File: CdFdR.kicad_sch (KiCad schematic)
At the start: 17 parts, among them J1 Moteur_1, J2 Moteur_2, J3 Moteur_3, J4 Moteur_4, U1 ESP32-S3-N16R8-DEVBOARD

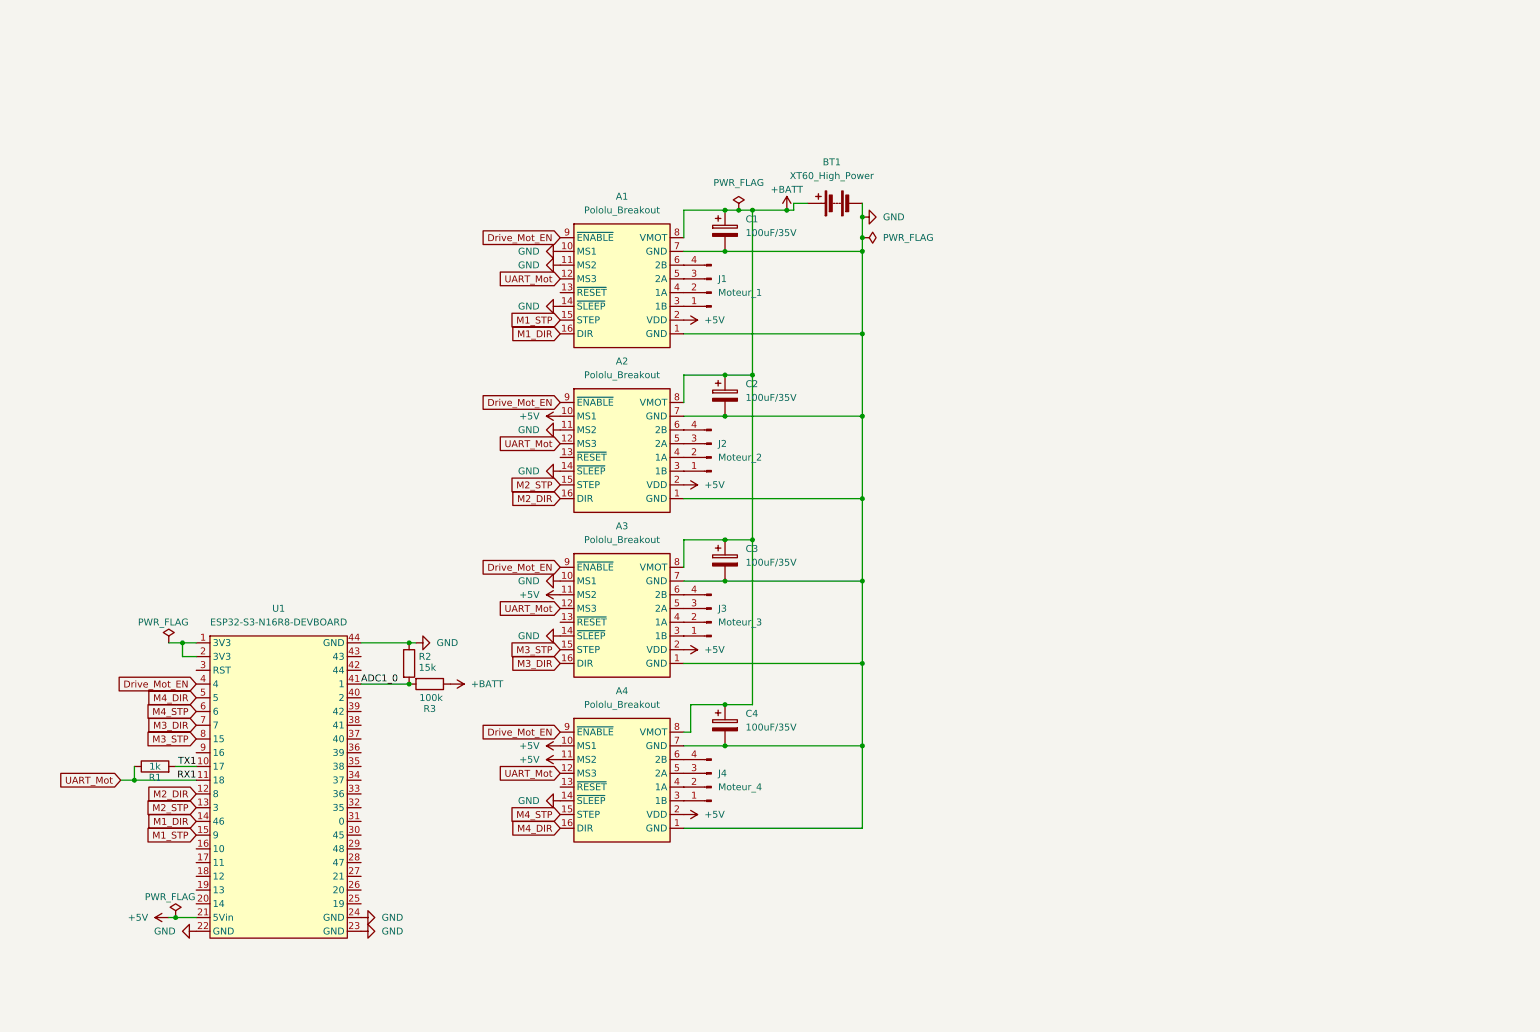
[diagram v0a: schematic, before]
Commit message: Ajout de composants
Ajout de composants sur le schématic
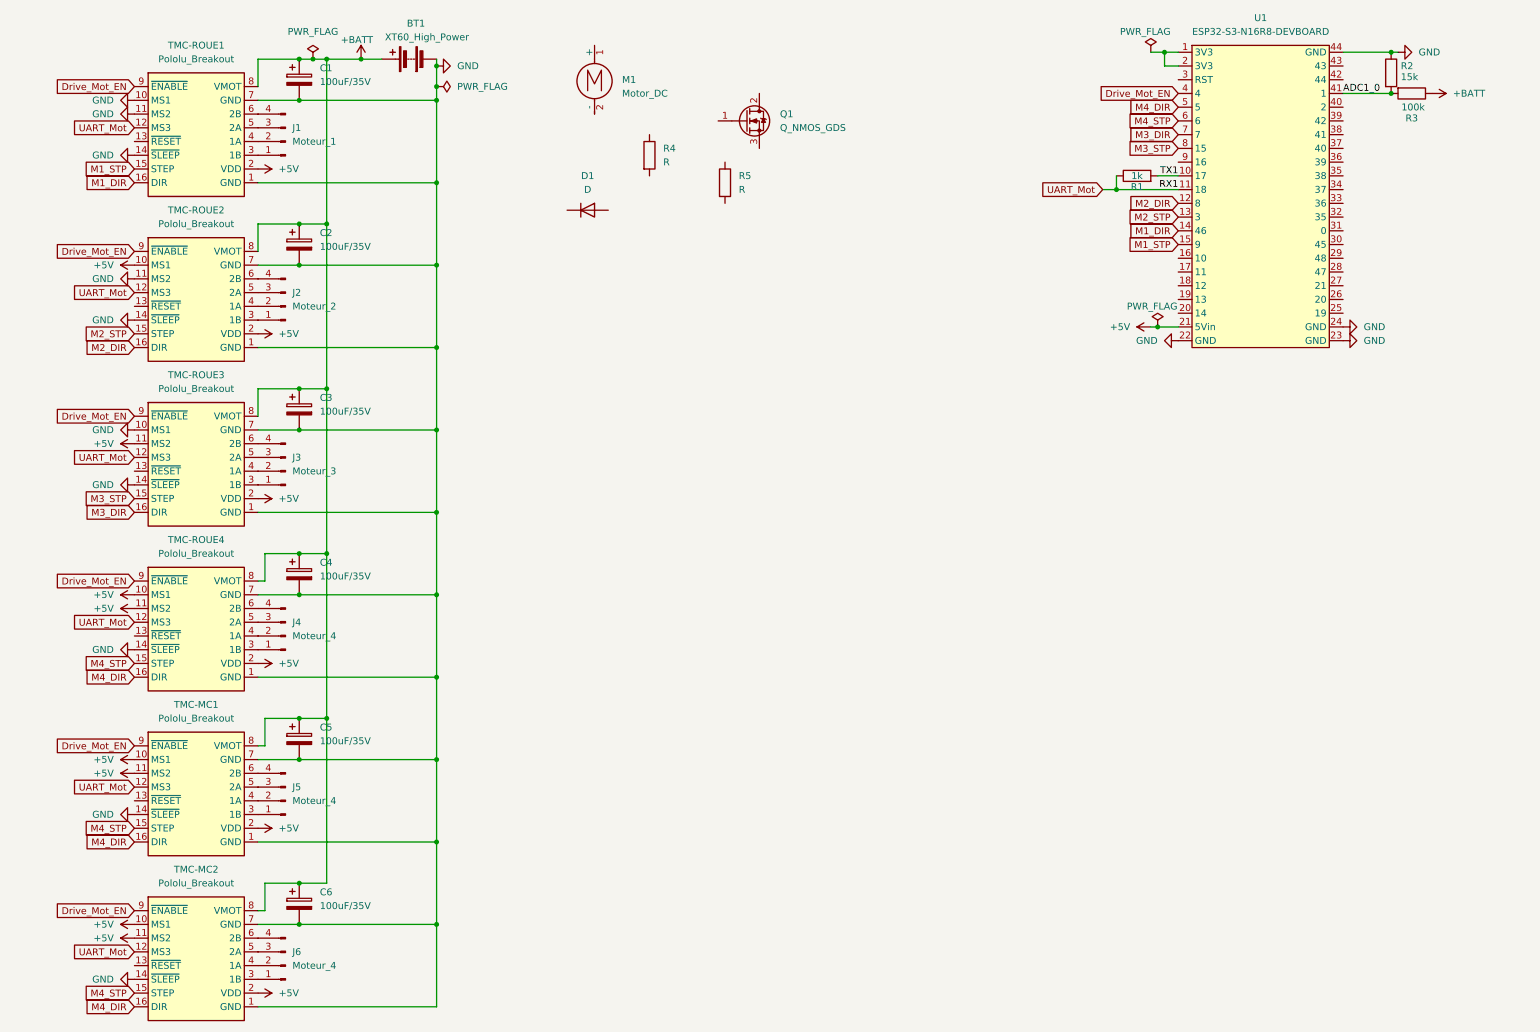
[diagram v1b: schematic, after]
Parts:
- added C5, C6: 100uF/35V, Capacitor_THT:CP_Radial_D6.3mm_P2.50mm, symbol Device:C_Polarized
- added D1: D, symbol Device:D
- added J5, J6: Moteur_4, Connector_PinHeader_2.54mm:PinHeader_1x04_P2.54mm_Vertical, symbol Connector:Conn_01x04_Pin
- added M1: Motor_DC, symbol Motor:Motor_DC
- added Q1: Q_NMOS_GDS, symbol Device:Q_NMOS_GDS
- added R4, R5: R, symbol Device:R
- added TMC-MC1, TMC-MC2: Pololu_Breakout, Custom:Pololu_Breakout-16_15.2x20.3mm_Better_Silkscreen, symbol Custom:Pololu_Breakout_Stepper_Driver
- renumbered A1 to TMC-ROUE1, A2 to TMC-ROUE2, A3 to TMC-ROUE3, A4 to TMC-ROUE4
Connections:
- net +5V: now also TMC-MC1.10 (MS1), TMC-MC1.11 (MS2), TMC-MC1.2 (VDD), TMC-MC2.10 (MS1), TMC-MC2.11 (MS2), TMC-MC2.2 (VDD)
- net +BATT: now also C5.1, C6.1, TMC-MC1.8 (VMOT), TMC-MC2.8 (VMOT)
- net Drive_Mot_EN: now also TMC-MC1.9 (~{ENABLE}), TMC-MC2.9 (~{ENABLE})
- net GND: now also C5.2, C6.2, TMC-MC1.1 (GND), TMC-MC1.14 (~{SLEEP}), TMC-MC1.7 (GND), TMC-MC2.1 (GND), TMC-MC2.14 (~{SLEEP}), TMC-MC2.7 (GND)
- net M4_DIR: now also TMC-MC1.16 (DIR), TMC-MC2.16 (DIR)
- net M4_STP: now also TMC-MC1.15 (STEP), TMC-MC2.15 (STEP)
- net UART_Mot: now also TMC-MC1.12 (MS3), TMC-MC2.12 (MS3)
- new net: J5.1 (Pin_1), TMC-MC1.3 (1B)
- new net: J5.2 (Pin_2), TMC-MC1.4 (1A)
- new net: J5.3 (Pin_3), TMC-MC1.5 (2A)
- new net: J5.4 (Pin_4), TMC-MC1.6 (2B)
- new net: J6.1 (Pin_1), TMC-MC2.3 (1B)
- new net: J6.2 (Pin_2), TMC-MC2.4 (1A)
- new net: J6.3 (Pin_3), TMC-MC2.5 (2A)
- new net: J6.4 (Pin_4), TMC-MC2.6 (2B)
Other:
- moved on the sheet: BT1, C1, C2, C3, C4, J1, J2, J3, J4, R1, R2, R3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

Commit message: Version envoyé pour vérif
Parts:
- removed M1: Motor_DC, symbol Motor:Motor_DC
- removed Q1: Q_NMOS_GDS, symbol Device:Q_NMOS_GDS
- added C7: 2200 uF, Capacitor_THT:CP_Radial_D16.0mm_P7.50mm, symbol Device:C_Polarized
- added D2, D3, D4: FR107, Diode_THT:D_DO-41_SOD81_P7.62mm_Horizontal, symbol Device:D
- added Electro1, Electro2: ElectroAimant, Connector_JST:JST_XH_B2B-XH-A_1x02_P2.50mm_Vertical, symbol Device:ElectromagneticActor
- added Fan1, Fan2: Fan, Connector_JST:JST_XH_B2B-XH-A_1x02_P2.50mm_Vertical, symbol Motor:Fan
- added H1, H2, H3, H4: MountingHole, MountingHole:MountingHole_3.2mm_M3, symbol Mechanical:MountingHole
- added J7: IHM, Connector_JST:JST_XH_B4B-XH-A_1x04_P2.50mm_Vertical, symbol Connector:Conn_01x04_Pin
- added J8: Lidar, Connector_JST:JST_XH_B4B-XH-A_1x04_P2.50mm_Vertical, symbol Connector:Conn_01x04_Pin
- added Module_LM2596: LM2596, Custom:LM2596 Converter DC-DC, symbol Custom:BuckConverter24-5
- added PUMP-1, PUMP-2: PUMP, Connector_JST:JST_XH_B2B-XH-A_1x02_P2.50mm_Vertical, symbol Motor:Motor_DC
- added Q1, Q2, Q3, Q4: IRLZ44N, Package_TO_SOT_THT:TO-220-3_Vertical, symbol Transistor_FET:IRLZ44N
- added R10, R6, R8: 330, Resistor_THT:R_Axial_DIN0207_L6.3mm_D2.5mm_P7.62mm_Horizontal, symbol Device:R
- added R11, R7, R9: 10k, Resistor_THT:R_Axial_DIN0207_L6.3mm_D2.5mm_P7.62mm_Horizontal, symbol Device:R
- added R12: 1k, Resistor_THT:R_Axial_DIN0207_L6.3mm_D2.5mm_P7.62mm_Horizontal, symbol Device:R
- added SW1: Alim_generale, Connector_AMASS:AMASS_XT60-F_1x02_P7.20mm_Vertical, symbol Switch:SW_Push
- added SW2: Tirette, Connector_JST:JST_XH_B2B-XH-A_1x02_P2.50mm_Vertical, symbol Switch:SW_Push
- added SW3: Urgence, Connector_AMASS:AMASS_XT60-F_1x02_P7.20mm_Vertical, symbol Switch:SW_Push
- added VALVE-1, VALVE-2: VALVE, Connector_JST:JST_XH_B2B-XH-A_1x02_P2.50mm_Vertical, symbol Motor:Motor_DC
- D1: value D -> FR107; footprint (none) -> Diode_THT:D_DO-41_SOD81_P7.62mm_Horizontal
- J1: value Moteur_1 -> Nema17_1; footprint Connector_PinHeader_2.54mm:PinHeader_1x04_P2.54mm_Vertical -> Connector_JST:JST_XH_B4B-XH-A_1x04_P2.50mm_Vertical
- J2: value Moteur_2 -> Nema17_2; footprint Connector_PinHeader_2.54mm:PinHeader_1x04_P2.54mm_Vertical -> Connector_JST:JST_XH_B4B-XH-A_1x04_P2.50mm_Vertical
- J3: value Moteur_3 -> Nema17_3; footprint Connector_PinHeader_2.54mm:PinHeader_1x04_P2.54mm_Vertical -> Connector_JST:JST_XH_B4B-XH-A_1x04_P2.50mm_Vertical
- J4: value Moteur_4 -> Nema17_4; footprint Connector_PinHeader_2.54mm:PinHeader_1x04_P2.54mm_Vertical -> Connector_JST:JST_XH_B4B-XH-A_1x04_P2.50mm_Vertical
- J5: value Moteur_4 -> Nema17_5; footprint Connector_PinHeader_2.54mm:PinHeader_1x04_P2.54mm_Vertical -> Connector_JST:JST_XH_B4B-XH-A_1x04_P2.50mm_Vertical
- J6: value Moteur_4 -> Nema17_6; footprint Connector_PinHeader_2.54mm:PinHeader_1x04_P2.54mm_Vertical -> Connector_JST:JST_XH_B4B-XH-A_1x04_P2.50mm_Vertical
- R1, R2, R3: footprint Resistor_THT:R_Axial_DIN0411_L9.9mm_D3.6mm_P15.24mm_Horizontal -> Resistor_THT:R_Axial_DIN0207_L6.3mm_D2.5mm_P7.62mm_Horizontal
- R4: value R -> 330; footprint (none) -> Resistor_THT:R_Axial_DIN0207_L6.3mm_D2.5mm_P7.62mm_Horizontal
- R5: value R -> 10k; footprint (none) -> Resistor_THT:R_Axial_DIN0207_L6.3mm_D2.5mm_P7.62mm_Horizontal
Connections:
- net +5V: now also J7.3 (Pin_3), J8.4 (Pin_4), Module_LM2596.3 (VOUT); no longer TMC-MC1.10 (MS1), TMC-MC1.11 (MS2), TMC-MC1.2 (VDD), TMC-MC2.10 (MS1), TMC-MC2.11 (MS2), TMC-MC2.2 (VDD), TMC-ROUE1.2 (VDD), TMC-ROUE2.10 (MS1), TMC-ROUE2.2 (VDD), TMC-ROUE3.11 (MS2), TMC-ROUE3.2 (VDD), TMC-ROUE4.10 (MS1), TMC-ROUE4.11 (MS2), TMC-ROUE4.2 (VDD)
- net Drive_Mot_EN: now also U1.8 (15); no longer TMC-MC1.9 (~{ENABLE}), TMC-MC2.9 (~{ENABLE}), U1.4
- net GND: now also R5.1, TMC-MC1.10 (MS1), TMC-MC1.11 (MS2), TMC-MC2.10 (MS1), C7.2, Fan1.2 (-), Fan2.2 (-), J7.4 (Pin_4), J8.2 (Pin_2), J8.3 (Pin_3), Module_LM2596.2 (GND), Module_LM2596.4 (GND), Q1.3 (S), Q2.3 (S), Q3.3 (S), Q4.3 (S), R11.1, R7.1, R9.1, SW2.2
- net M1_DIR: now also U1.4; no longer U1.14 (46)
- net M1_STP: now also U1.5; no longer U1.15 (9)
- net M2_DIR: now also U1.6; no longer U1.12 (8)
- net M2_STP: now also U1.7; no longer U1.13 (3)
- net M3_DIR: now also U1.12 (8); no longer U1.7
- net M3_STP: now also U1.13 (3); no longer U1.8 (15)
- net M4_DIR: now also U1.15 (9); no longer TMC-MC1.16 (DIR), TMC-MC2.16 (DIR), U1.5
- net M4_STP: now also U1.16 (10); no longer TMC-MC1.15 (STEP), TMC-MC2.15 (STEP), U1.6
- net UART_Mot: now also R1.2; no longer R1.1, TMC-MC1.12 (MS3), TMC-MC2.12 (MS3)
- net at R5.2: now also R4.2, Q1.1 (G)
- net +24V: now reaches D1.1 (K)
- net +24V: now also C1.1, C2.1, C3.1, C4.1, C5.1, C6.1, TMC-MC1.8 (VMOT), TMC-MC2.8 (VMOT), TMC-ROUE1.8 (VMOT), TMC-ROUE2.8 (VMOT), TMC-ROUE3.8 (VMOT), TMC-ROUE4.8 (VMOT), D2.1 (K), D3.1 (K), D4.1 (K), Electro1.2 (+), Electro2.2 (+), Fan1.1 (+), Fan2.1 (+), PUMP-1.1 (+), PUMP-2.1 (+), SW3.1, VALVE-1.1 (+), VALVE-2.1 (+)
- net at D1.2 (A): now also PUMP-1.2 (-), Q1.2 (D), VALVE-1.2 (-)
- net PUMP_VALVE1: now reaches R4.1
- net PUMP_VALVE1: now also U1.36 (39)
- net +3.3V: now reaches U1.1 (3V3), U1.2 (3V3)
- net +3.3V: now also TMC-MC1.2 (VDD), TMC-MC2.11 (MS2), TMC-MC2.2 (VDD), TMC-ROUE1.2 (VDD), TMC-ROUE2.10 (MS1), TMC-ROUE2.2 (VDD), TMC-ROUE3.11 (MS2), TMC-ROUE3.2 (VDD), TMC-ROUE4.10 (MS1), TMC-ROUE4.11 (MS2), TMC-ROUE4.2 (VDD)
- net M5_DIR: now reaches U1.17 (11)
- net M5_DIR: now also TMC-MC1.16 (DIR)
- net M5_STP: now reaches U1.18 (12)
- net M5_STP: now also TMC-MC1.15 (STEP)
- net M6_DIR: now reaches U1.19 (13)
- net M6_DIR: now also TMC-MC2.16 (DIR)
- net M6_STP: now reaches U1.20 (14)
- net M6_STP: now also TMC-MC2.15 (STEP)
- net at U1.27 (21): now also SW2.1
- net ELECTRO2: now reaches U1.28 (47)
- net ELECTRO2: now also R10.1
- net ELECTRO1: now reaches U1.29 (48)
- net ELECTRO1: now also R8.1
- net PUMP_VALVE2: now reaches U1.35 (38)
- net PUMP_VALVE2: now also R6.1
- net CLK_IHM: now reaches U1.37 (40)
- net CLK_IHM: now also J7.1 (Pin_1)
- net DIO_IHM: now reaches U1.38 (41)
- net DIO_IHM: now also J7.2 (Pin_2)
- net at U1.39 (42): now also R12.2
- net UART_Chariot: now reaches U1.40 (2)
- net UART_Chariot: now also TMC-MC1.12 (MS3), TMC-MC2.12 (MS3), R12.1
- net TX_Lidar: now reaches U1.42 (44)
- net TX_Lidar: now also J8.1 (Pin_1)
- net Drive_Chariot_EN: now reaches U1.9 (16)
- net Drive_Chariot_EN: now also TMC-MC1.9 (~{ENABLE}), TMC-MC2.9 (~{ENABLE})
- removed net +BATT: BT1.1 (+), C1.1, C2.1, C3.1, C4.1, C5.1, C6.1, R3.1, TMC-MC1.8 (VMOT), TMC-MC2.8 (VMOT), TMC-ROUE1.8 (VMOT), TMC-ROUE2.8 (VMOT), TMC-ROUE3.8 (VMOT), TMC-ROUE4.8 (VMOT)
- net TX1: no longer names the net of U1.10 (17)
- net TX1: now also R1.1; no longer R1.2
- new net: Q4.1 (G), R10.2, R11.2
- new net: D4.2 (A), Electro2.1 (-), Q4.2 (D)
- new net: BT1.1 (+), SW1.1
- new net: D2.2 (A), PUMP-2.2 (-), Q2.2 (D), VALVE-2.2 (-)
- new net: Q2.1 (G), R6.2, R7.2
- new net: D3.2 (A), Electro1.1 (-), Q3.2 (D)
- new net: Q3.1 (G), R8.2, R9.2
- new net V_Batt: C7.1, Module_LM2596.1 (VIN), R3.1, SW1.2, SW3.2
- no-connect marks 0 -> 16
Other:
- note added: "RX1"
- note added: "RX2"
- note added: "TX1"
- note added: "TX2"
- company: Valentin G. -> Centrale Lille Makers
- moved on the sheet: BT1, R1, R2, R3
